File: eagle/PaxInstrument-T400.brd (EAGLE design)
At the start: 99.1 x 50.8 mm, 115 parts, among them IC1 MCP3424, J1 MICRO-SDCARD-CONNECTOR-330006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, U1 MCP9800, U3 MCP73831, U4 MIC5219-3.3V, U8 NC7S32, X1 FH12-12S-0.5SH, Y1 RESONATORSMD

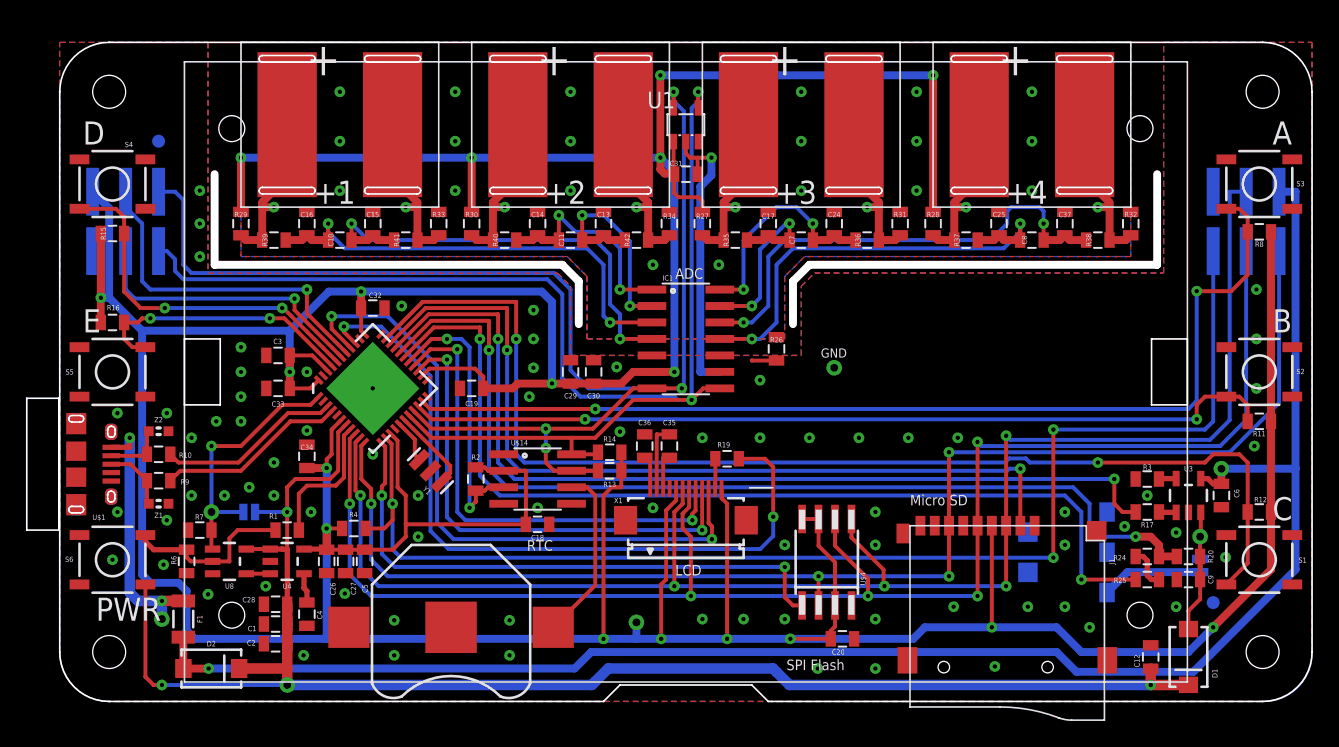
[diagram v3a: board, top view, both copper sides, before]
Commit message: Updated PCB and Library for Rev 0.9
-Updated Thermocouple connector milled slots close to footprint edge
(issue #111)
-Added restricted area under milled slots to prevent short circuit
-modify milling slot (> 0.8mm) to meet PCB factory capability
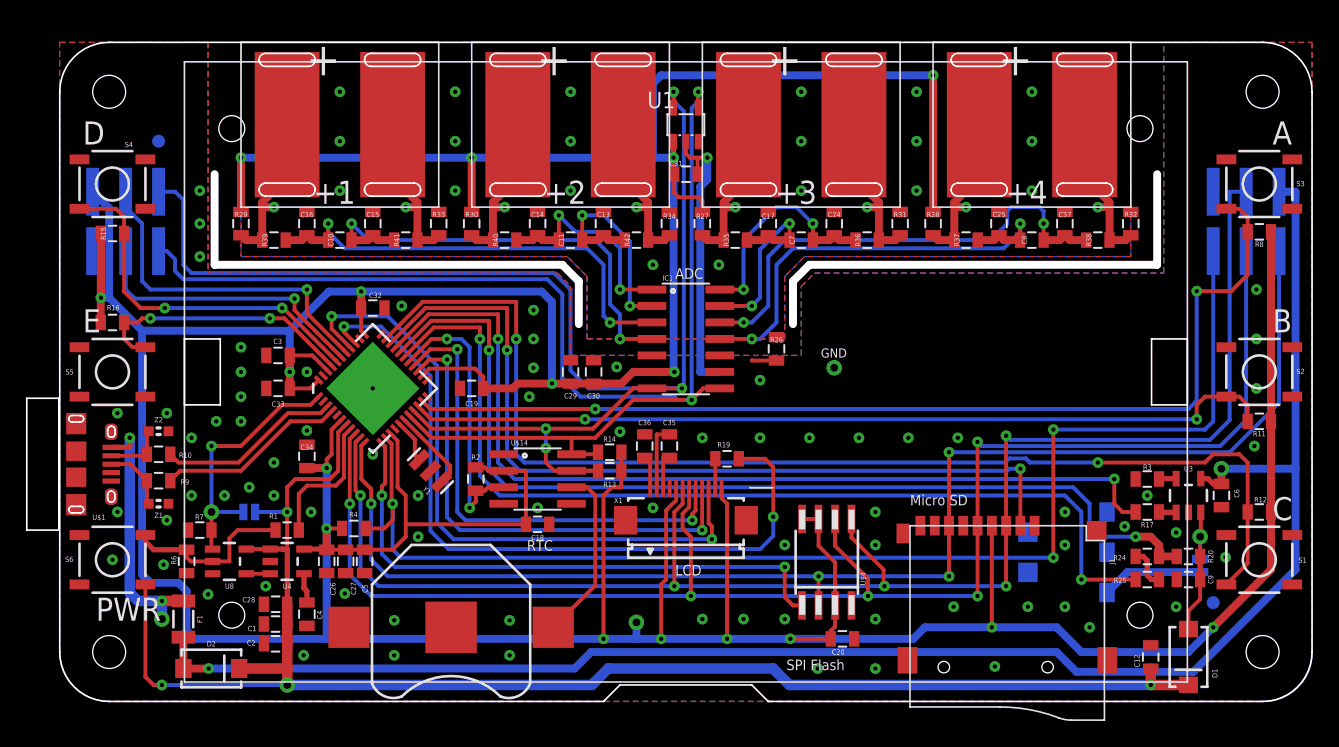
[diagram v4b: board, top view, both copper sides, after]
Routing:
- net 3.3V: track 463.9 -> 462.7 mm, vias 18 -> 17
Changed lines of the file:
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@@
 <layer number="14" name="Route14" color="1" fill="6" visible="no" active="no"/>
 <layer number="15" name="Route15" color="4" fill="6" visible="no" active="no"/>
-<layer number="16" name="Bottom" color="1" fill="1" visible="yes" active="yes"/>
+<layer number="16" name="Bottom" color="1" fill="1" visible="no" active="yes"/>
 <layer number="17" name="Pads" color="2" fill="1" visible="yes" active="yes"/>
 <layer number="18" name="Vias" color="2" fill="1" visible="yes" active="yes"/>
@@
 <layer number="20" name="Dimension" color="13" fill="1" visible="yes" active="yes"/>
 <layer number="21" name="tPlace" color="7" fill="1" visible="yes" active="yes"/>
-<layer number="22" name="bPlace" color="14" fill="1" visible="yes" active="yes"/>
+<layer number="22" name="bPlace" color="14" fill="1" visible="no" active="yes"/>
 <layer number="23" name="tOrigins" color="15" fill="1" visible="yes" active="yes"/>
 <layer number="24" name="bOrigins" color="15" fill="1" visible="yes" active="yes"/>
@@
 <layer number="27" name="tValues" color="7" fill="1" visible="no" active="yes"/>
 <layer number="28" name="bValues" color="7" fill="1" visible="yes" active="yes"/>
-<layer number="29" name="tStop" color="7" fill="3" visible="no" active="yes"/>
+<layer number="29" name="tStop" color="7" fill="3" visible="yes" active="yes"/>
 <layer number="30" name="bStop" color="7" fill="6" visible="no" active="yes"/>
-<layer number="31" name="tCream" color="7" fill="4" visible="no" active="yes"/>
+<layer number="31" name="tCream" color="7" fill="4" visible="yes" active="yes"/>
 <layer number="32" name="bCream" color="7" fill="5" visible="no" active="yes"/>
 <layer number="33" name="tFinish" color="6" fill="3" visible="no" active="yes"/>
@@
 <contactref element="C18" pad="1"/>
 <wire x1="20.574" y1="11.745" x2="20.574" y2="11.695" width="0.6096" layer="1"/>
-<wire x1="47.31" y1="43.15" x2="47.31" y2="40.69" width="0.3048" layer="1"/>
-<wire x1="47.31" y1="40.69" x2="47.36" y2="40.64" width="0.3048" layer="1"/>
 <wire x1="45.6438" y1="25.4" x2="44.196" y2="25.4" width="0.6096" layer="1"/>
 <wire x1="44.196" y1="25.4" x2="43.296" y2="24.5" width="0.6096" layer="1"/>
@@
 <wire x1="67.31" y1="37.73" x2="67.31" y2="48.26" width="0.6096" layer="1"/>
 <via x="67.31" y="48.26" extent="1-16" drill="0.3302"/>
-<wire x1="67.31" y1="48.26" x2="46.2915" y2="48.26" width="0.6096" layer="16"/>
-<via x="46.2915" y="48.26" extent="1-16" drill="0.3302"/>
+<wire x1="67.31" y1="48.26" x2="46.355" y2="48.26" width="0.6096" layer="16"/>
 <wire x1="20.524" y1="11.745" x2="20.574" y2="11.695" width="0.6096" layer="1"/>
 <wire x1="31.75" y1="41.91" x2="13.97" y2="41.91" width="0.6096" layer="16"/>
@@
 <wire x1="49.53" y1="38.5445" x2="49.2125" y2="38.862" width="0.3048" layer="1"/>
 <wire x1="49.2125" y1="38.862" x2="47.6775" y2="38.862" width="0.3048" layer="1"/>
-<via x="46.2915" y="41.91" extent="1-16" drill="0.3302"/>
-<wire x1="46.2915" y1="48.26" x2="46.2915" y2="41.91" width="0.6096" layer="1"/>
+<via x="47.31" y="41.91" extent="1-16" drill="0.3302"/>
 <contactref element="TP13" pad="P$1"/>
 <contactref element="GND" pad="42"/>
@@
 <wire x1="3.164" y1="36.195" x2="3.164" y2="36.068" width="0.6096" layer="1"/>
 <contactref element="ICSP1" pad="6"/>
-<wire x1="47.371" y1="40.8305" x2="47.371" y2="25.4" width="0.6096" layer="16"/>
 <via x="47.371" y="25.4" extent="1-16" drill="0.3302"/>
 <wire x1="47.371" y1="25.4" x2="45.6438" y2="25.4" width="0.6096" layer="1"/>
@@
 <wire x1="34.925" y1="24.13" x2="35.295" y2="24.5" width="0.6096" layer="1"/>
 <wire x1="35.295" y1="24.5" x2="37.94125" y2="24.5" width="0.6096" layer="1"/>
-<wire x1="31.75" y1="41.91" x2="46.2915" y2="41.91" width="0.6096" layer="16"/>
+<wire x1="31.75" y1="41.91" x2="45.72" y2="41.91" width="0.6096" layer="16"/>
+<wire x1="45.72" y1="41.91" x2="47.31" y2="41.91" width="0.6096" layer="16"/>
 <wire x1="31.75" y1="41.91" x2="31.75" y2="37.73" width="0.6096" layer="1"/>
 <wire x1="57.2135" y1="14.0615" x2="58.4835" y2="14.0615" width="0.3048" layer="1"/>
@@
 <wire x1="59.425" y1="4.826" x2="59.425" y2="5.45" width="0.3048" layer="1"/>
 <wire x1="59.425" y1="5.45" x2="59.7535" y2="5.7785" width="0.3048" layer="1"/>
-<wire x1="47.371" y1="40.8305" x2="46.2915" y2="41.91" width="0.6096" layer="16"/>
-<wire x1="47.31" y1="40.69" x2="46.609" y2="40.69" width="0.6096" layer="1"/>
-<wire x1="46.609" y1="40.69" x2="46.2915" y2="41.0075" width="0.6096" layer="1"/>
-<wire x1="46.2915" y1="41.0075" x2="46.2915" y2="41.91" width="0.6096" layer="1"/>
 <wire x1="46.355" y1="4.826" x2="44.45" y2="4.826" width="0.6096" layer="16"/>
 <wire x1="44.45" y1="4.826" x2="41.91" y2="4.826" width="0.6096" layer="16"/>
 <wire x1="44.45" y1="6.096" x2="44.45" y2="4.826" width="0.6096" layer="16"/>
+<wire x1="46.355" y1="48.26" x2="45.72" y2="47.625" width="0.6096" layer="16"/>
+<wire x1="45.72" y1="47.625" x2="45.72" y2="41.91" width="0.6096" layer="16"/>
+<wire x1="47.31" y1="41.91" x2="47.31" y2="25.461" width="0.6096" layer="16"/>
+<wire x1="47.31" y1="25.461" x2="47.371" y2="25.4" width="0.6096" layer="16"/>
+<wire x1="47.31" y1="43.15" x2="47.31" y2="41.91" width="0.4064" layer="1"/>
+<wire x1="47.31" y1="41.91" x2="47.31" y2="40.69" width="0.4064" layer="1"/>
+<wire x1="47.31" y1="40.69" x2="47.36" y2="40.64" width="0.4064" layer="1"/>
 </signal>
 <signal name="3V3EN">
@@
 <wire x1="48.26" y1="42.2275" x2="48.5775" y2="41.91" width="0.3048" layer="1"/>
 <via x="19.05" y="25.4" extent="1-16" drill="0.3302"/>
-<via x="50.2285" y="41.91" extent="1-16" drill="0.3302"/>
+<via x="49.911" y="41.91" extent="1-16" drill="0.3302"/>
 <wire x1="53.34" y1="26.289" x2="53.34" y2="26.278" width="0.3048" layer="1"/>
 <wire x1="53.34" y1="26.278" x2="55.245" y2="26.278" width="0.3048" layer="1"/>
@@
 <via x="36.5125" y="27.94" extent="1-16" drill="0.3302"/>
 <via x="36.83" y="14.9225" extent="1-16" drill="0.3302"/>
-<wire x1="50.2285" y1="41.91" x2="50.2285" y2="40.54475" width="0.6096" layer="16"/>
 <wire x1="49.37125" y1="39.6875" x2="49.37125" y2="25.4" width="0.6096" layer="16"/>
 <wire x1="49.37125" y1="25.4" x2="50.8762" y2="25.4" width="0.6096" layer="16"/>
 <wire x1="48.5775" y1="41.91" x2="49.16" y2="41.91" width="0.3048" layer="1"/>
 <wire x1="49.16" y1="40.64" x2="49.16" y2="41.91" width="0.3048" layer="1"/>
-<wire x1="49.16" y1="41.91" x2="50.2285" y2="41.91" width="0.3048" layer="1"/>
+<wire x1="49.16" y1="41.91" x2="49.911" y2="41.91" width="0.3048" layer="1"/>
 <via x="27.6225" y="12.7" extent="1-16" drill="0.3302"/>
 <via x="13.97" y="23.495" extent="1-16" drill="0.3302"/>
@@
 <via x="58.42" y="2.54" extent="1-16" drill="0.3302"/>
 <via x="62.865" y="2.54" extent="1-16" drill="0.3302"/>
-<wire x1="50.2285" y1="40.54475" x2="49.37125" y2="39.6875" width="0.6096" layer="16"/>
+<wire x1="49.911" y1="41.91" x2="49.911" y2="40.22725" width="0.6096" layer="16"/>
+<wire x1="49.911" y1="40.22725" x2="49.37125" y2="39.6875" width="0.6096" layer="16"/>
 </signal>
 <signal name="USBVCC">

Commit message: Updated Gerber and PCB for Rev 0.9
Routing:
- net SW_C: track 90.5 -> 89.4 mm
- net SD_CS: track 66.1 -> 65.2 mm
- net BATT_STAT: track 72.3 -> 71.6 mm
- net VBAT_SENSE: track 76.6 -> 76.0 mm
- net VBAT_EN: track 75.1 -> 74.6 mm
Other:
- outline, holes or cut-outs redrawn
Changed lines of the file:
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@@
 <setting verticaltext="up"/>
 </settings>
-<grid distance="25" unitdist="mil" unit="mil" style="lines" multiple="1" display="yes" altdistance="6.25" altunitdist="mil" altunit="mil"/>
+<grid distance="25" unitdist="mil" unit="mm" style="lines" multiple="1" display="yes" altdistance="6.25" altunitdist="mil" altunit="mil"/>
 <layers>
 <layer number="1" name="Top" color="4" fill="1" visible="yes" active="yes"/>
@@
 <layer number="14" name="Route14" color="1" fill="6" visible="no" active="no"/>
 <layer number="15" name="Route15" color="4" fill="6" visible="no" active="no"/>
-<layer number="16" name="Bottom" color="1" fill="1" visible="no" active="yes"/>
+<layer number="16" name="Bottom" color="1" fill="1" visible="yes" active="yes"/>
 <layer number="17" name="Pads" color="2" fill="1" visible="yes" active="yes"/>
 <layer number="18" name="Vias" color="2" fill="1" visible="yes" active="yes"/>
@@
 <layer number="20" name="Dimension" color="13" fill="1" visible="yes" active="yes"/>
 <layer number="21" name="tPlace" color="7" fill="1" visible="yes" active="yes"/>
-<layer number="22" name="bPlace" color="14" fill="1" visible="no" active="yes"/>
+<layer number="22" name="bPlace" color="14" fill="1" visible="yes" active="yes"/>
 <layer number="23" name="tOrigins" color="15" fill="1" visible="yes" active="yes"/>
 <layer number="24" name="bOrigins" color="15" fill="1" visible="yes" active="yes"/>
@@
 <layer number="27" name="tValues" color="7" fill="1" visible="no" active="yes"/>
 <layer number="28" name="bValues" color="7" fill="1" visible="yes" active="yes"/>
-<layer number="29" name="tStop" color="7" fill="3" visible="yes" active="yes"/>
+<layer number="29" name="tStop" color="7" fill="3" visible="no" active="yes"/>
 <layer number="30" name="bStop" color="7" fill="6" visible="no" active="yes"/>
-<layer number="31" name="tCream" color="7" fill="4" visible="yes" active="yes"/>
+<layer number="31" name="tCream" color="7" fill="4" visible="no" active="yes"/>
 <layer number="32" name="bCream" color="7" fill="5" visible="no" active="yes"/>
 <layer number="33" name="tFinish" color="6" fill="3" visible="no" active="yes"/>
@@
 <wire x1="3.81" y1="50.8" x2="92.71" y2="50.8" width="0.127" layer="20"/>
 <wire x1="96.52" y1="46.99" x2="96.52" y2="3.81" width="0.127" layer="20"/>
-<wire x1="84.582" y1="33.655" x2="57.785" y2="33.655" width="0.6096" layer="46"/>
-<wire x1="11.938" y1="33.655" x2="38.735" y2="33.655" width="0.6096" layer="46"/>
-<wire x1="57.785" y1="33.655" x2="56.515" y2="32.385" width="0.6096" layer="46"/>
-<wire x1="56.515" y1="32.385" x2="56.515" y2="29.083" width="0.6096" layer="46"/>
-<wire x1="38.735" y1="33.655" x2="40.005" y2="32.385" width="0.6096" layer="46"/>
-<wire x1="40.005" y1="32.385" x2="40.005" y2="29.083" width="0.6096" layer="46"/>
+<wire x1="84.582" y1="33.9725" x2="57.785" y2="33.9725" width="0.8128" layer="46"/>
+<wire x1="57.785" y1="33.9725" x2="56.515" y2="32.7025" width="0.8128" layer="46"/>
+<wire x1="56.515" y1="32.7025" x2="56.515" y2="29.083" width="0.8128" layer="46"/>
+<wire x1="11.938" y1="33.9725" x2="38.735" y2="33.9725" width="0.8128" layer="46"/>
+<wire x1="38.735" y1="33.9725" x2="40.005" y2="32.7025" width="0.8128" layer="46"/>
+<wire x1="40.005" y1="32.7025" x2="40.005" y2="29.083" width="0.8128" layer="46"/>
 <wire x1="96.52" y1="46.99" x2="92.71" y2="50.8" width="0.127" layer="20" curve="90"/>
 <wire x1="3.81" y1="50.8" x2="0" y2="46.99" width="0.127" layer="20" curve="90"/>
@@
 <text x="1.778" y="28.448" size="1.778" layer="21" font="vector" ratio="15">E</text>
 <text x="2.794" y="6.223" size="1.778" layer="21" font="vector" ratio="15">PWR</text>
-<wire x1="84.582" y1="40.64" x2="84.582" y2="33.655" width="0.6096" layer="46"/>
-<wire x1="11.938" y1="33.655" x2="11.938" y2="40.64" width="0.6096" layer="46"/>
+<wire x1="84.582" y1="40.64" x2="84.582" y2="33.9725" width="0.8128" layer="46"/>
+<wire x1="11.938" y1="33.9725" x2="11.938" y2="40.64" width="0.8128" layer="46"/>
 <dimension x1="-3.81" y1="0" x2="-3.81" y2="3.81" x3="-6.35" y3="1.905" textsize="1.778" textratio="15" layer="47" dtype="vertical" unit="inch"/>
 <dimension x1="-3.81" y1="0" x2="-3.81" y2="10.922" x3="-22.86" y3="5.461" textsize="1.778" textratio="15" layer="47" dtype="vertical" unit="inch"/>
@@
 <vertex x="0" y="50.8"/>
 <vertex x="11.43" y="50.8"/>
-<vertex x="11.43" y="33.02"/>
-<vertex x="38.354" y="33.02"/>
-<vertex x="39.37" y="32.004"/>
+<vertex x="11.43" y="33.655"/>
+<vertex x="38.354" y="33.655"/>
+<vertex x="39.37" y="32.639"/>
 <vertex x="39.37" y="26.67"/>
 <vertex x="57.15" y="26.67"/>
-<vertex x="57.15" y="32.004"/>
-<vertex x="58.166" y="33.02"/>
-<vertex x="85.09" y="33.02"/>
+<vertex x="57.15" y="32.639"/>
+<vertex x="58.166" y="33.655"/>
+<vertex x="85.09" y="33.655"/>
 <vertex x="85.09" y="50.8"/>
 </polygon>
@@
 <vertex x="0" y="50.8"/>
 <vertex x="11.43" y="50.8"/>
-<vertex x="11.43" y="33.02"/>
-<vertex x="38.354" y="33.02"/>
-<vertex x="39.37" y="32.004"/>
+<vertex x="11.43" y="33.655"/>
+<vertex x="38.354" y="33.655"/>
+<vertex x="39.37" y="32.639"/>
 <vertex x="39.37" y="26.67"/>
 <vertex x="57.15" y="26.67"/>
-<vertex x="57.15" y="32.004"/>
-<vertex x="58.166" y="33.02"/>
-<vertex x="85.09" y="33.02"/>
+<vertex x="57.15" y="32.639"/>
+<vertex x="58.166" y="33.655"/>
+<vertex x="85.09" y="33.655"/>
 <vertex x="85.09" y="50.8"/>
 </polygon>
@@
 <wire x1="74.039" y1="17.93875" x2="73.18375" y2="17.93875" width="0.3048" layer="16"/>
 <wire x1="73.18375" y1="17.93875" x2="73.025" y2="17.78" width="0.3048" layer="16"/>
-<wire x1="28.199928125" y1="30.32125" x2="34.4805" y2="30.32125" width="0.3048" layer="1"/>
-<wire x1="34.4805" y1="30.32125" x2="34.4805" y2="27.08275" width="0.3048" layer="1"/>
+<wire x1="28.199928125" y1="30.32125" x2="32.9805" y2="30.32125" width="0.3048" layer="1"/>
+<wire x1="32.9805" y1="30.32125" x2="34.4805" y2="28.82125" width="0.3048" layer="1"/>
+<wire x1="34.4805" y1="28.82125" x2="34.4805" y2="27.08275" width="0.3048" layer="1"/>
 </signal>
 <signal name="PWR_ONOFF">
@@
 <wire x1="35.814" y1="18.415" x2="72.86625" y2="18.415" width="0.3048" layer="16"/>
 <wire x1="72.86625" y1="18.415" x2="73.18375" y2="18.7325" width="0.3048" layer="16"/>
-<wire x1="35.179" y1="30.7975" x2="35.179" y2="27.94" width="0.3048" layer="1"/>
+<wire x1="27.969071875" y1="30.7975" x2="33.379" y2="30.7975" width="0.3048" layer="1"/>
+<wire x1="33.379" y1="30.7975" x2="35.179" y2="28.9975" width="0.3048" layer="1"/>
+<wire x1="35.179" y1="28.9975" x2="35.179" y2="27.94" width="0.3048" layer="1"/>
 <wire x1="25.119946875" y1="27.948375" x2="27.969071875" y2="30.7975" width="0.3048" layer="1"/>
-<wire x1="27.969071875" y1="30.7975" x2="35.179" y2="30.7975" width="0.3048" layer="1"/>
 </signal>
 <signal name="SW_A">
@@
 <contactref element="GND" pad="30"/>
 <wire x1="25.82705625" y1="27.24126875" x2="28.4307875" y2="29.845" width="0.3048" layer="1"/>
-<wire x1="28.4307875" y1="29.845" x2="33.782" y2="29.845" width="0.3048" layer="1"/>
+<wire x1="28.4307875" y1="29.845" x2="32.512" y2="29.845" width="0.3048" layer="1"/>
+<wire x1="32.512" y1="29.845" x2="33.782" y2="28.575" width="0.3048" layer="1"/>
+<wire x1="33.782" y1="28.575" x2="33.782" y2="27.94" width="0.3048" layer="1"/>
 <via x="33.782" y="27.94" extent="1-16" drill="0.3302"/>
-<wire x1="33.782" y1="29.845" x2="33.782" y2="27.94" width="0.3048" layer="1"/>
 </signal>
 <signal name="USB_VCC">
@@
 <wire x1="26.180609375" y1="26.887715625" x2="28.62989375" y2="29.337" width="0.3048" layer="1"/>
 <via x="33.0835" y="27.08275" extent="1-16" drill="0.3302"/>
-<wire x1="28.62989375" y1="29.337" x2="33.0835" y2="29.337" width="0.3048" layer="1"/>
-<wire x1="33.0835" y1="29.337" x2="33.0835" y2="27.08275" width="0.3048" layer="1"/>
+<wire x1="28.62989375" y1="29.337" x2="32.0835" y2="29.337" width="0.3048" layer="1"/>
+<wire x1="32.0835" y1="29.337" x2="33.0835" y2="28.337" width="0.3048" layer="1"/>
+<wire x1="33.0835" y1="28.337" x2="33.0835" y2="27.08275" width="0.3048" layer="1"/>
 </signal>
 <signal name="DATA2">
@@
 <via x="32.385" y="27.94" extent="1-16" drill="0.3302"/>
 <wire x1="26.5341625" y1="26.5341625" x2="28.829" y2="28.829" width="0.3048" layer="1"/>
-<wire x1="28.829" y1="28.829" x2="32.385" y2="28.829" width="0.3048" layer="1"/>
-<wire x1="32.385" y1="28.829" x2="32.385" y2="27.94" width="0.3048" layer="1"/>
+<wire x1="28.829" y1="28.829" x2="31.496" y2="28.829" width="0.3048" layer="1"/>
+<wire x1="31.496" y1="28.829" x2="32.385" y2="27.94" width="0.3048" layer="1"/>
 </signal>
 <signal name="N$4">
